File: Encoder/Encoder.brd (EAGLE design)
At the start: 100 x 80 mm, 4 parts, among them IC1 4017D

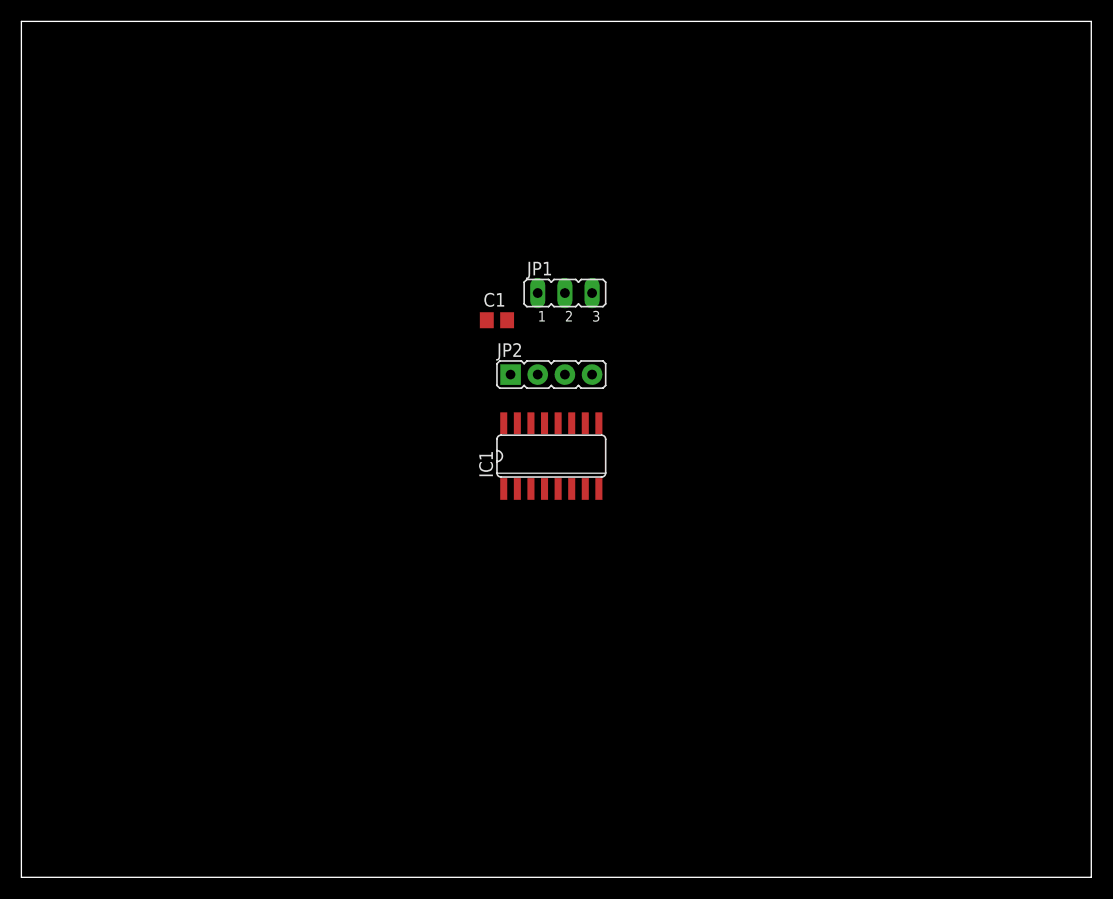
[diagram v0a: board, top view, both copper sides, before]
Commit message: Added a pcb for encoder: made scheme, library and prearranged components on the board
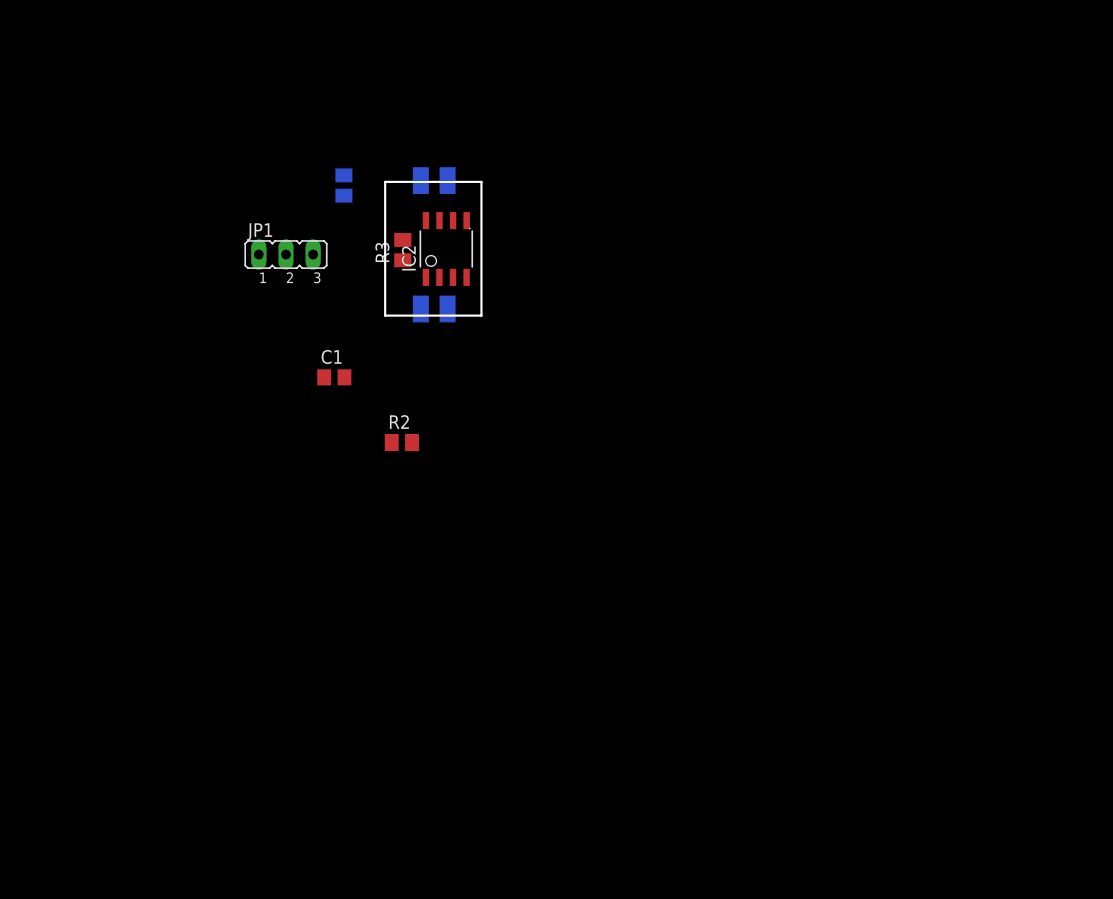
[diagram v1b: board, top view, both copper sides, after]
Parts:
- removed IC1: 4017D, 40xx:SO16
- removed JP2: PLS-(1х4), jumper:PLS-(1х4)
- added IC2: TINY13-20SSU, atmel:8S1
- added R1: (no value), rcl:M0805
- added R2, R3: 10k, rcl:M0805
- added U$1: ITR-9608, EncoderLib:ITR-9608-FOOTPRINT
- C1: value (none) -> 0.1u
- moved JP1 26.3 mm to (24.7, 58.2)
- moved C1 16.1 mm to (29.2, 46.7)
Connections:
- removed net VDD: IC1.16
- removed net VSS: IC1.8
- new net !RES: IC2.1, R3.1
- new net +5V: C1.1, IC2.8, JP1.3, R1.2, R2.2, R3.2
- new net DATA-IN: IC2.5, R2.1, U$1.C
- new net DATA-OUT: IC2.3, JP1.2
- new net GND: C1.2, IC2.4, JP1.1, U$1.E, U$1.K
- new net N$2: R1.1, U$1.A
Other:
- board size 100 x 80 mm -> 9 x 12.5 mm
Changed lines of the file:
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@@
 <setting verticaltext="up"/>
 </settings>
-<grid distance="50" unitdist="mil" unit="mil" style="lines" multiple="1" display="no" altdistance="5" altunitdist="mil" altunit="mil"/>
+<grid distance="0.003125" unitdist="mic" unit="mm" style="lines" multiple="1" display="no" altdistance="5" altunitdist="mil" altunit="mil"/>
 <layers>
 <layer number="1" name="Top" color="4" fill="1" visible="yes" active="yes"/>
@@
 <board>
 <plain>
-<wire x1="0" y1="0" x2="100" y2="0" width="0" layer="20"/>
-<wire x1="100" y1="0" x2="100" y2="80" width="0" layer="20"/>
-<wire x1="100" y1="80" x2="0" y2="80" width="0" layer="20"/>
-<wire x1="0" y1="80" x2="0" y2="0" width="0" layer="20"/>
+<wire x1="0" y1="0" x2="100" y2="0" width="0" layer="49"/>
+<wire x1="100" y1="0" x2="100" y2="80" width="0" layer="49"/>
+<wire x1="100" y1="80" x2="0" y2="80" width="0" layer="49"/>
+<wire x1="0" y1="80" x2="0" y2="0" width="0" layer="49"/>
+<wire x1="34" y1="65" x2="43" y2="65" width="0.2" layer="20"/>
+<wire x1="34" y1="52.5" x2="34" y2="65" width="0.2" layer="20"/>
+<wire x1="43" y1="65" x2="43" y2="52.5" width="0.2" layer="20"/>
+<wire x1="43" y1="52.5" x2="34" y2="52.5" width="0.2" layer="20"/>
 </plain>
 <attributes>
@@
 </autorouter>
 <elements>
-<element name="C1" library="rcl" library_urn="urn:adsk.eagle:library:334" package="C0805" package3d_urn="urn:adsk.eagle:package:23617/2" value="" x="44.45" y="52.07" smashed="yes">
-<attribute name="NAME" x="43.18" y="53.34" size="1.27" layer="25"/>
-<attribute name="POPULARITY" value="88" x="68.58" y="34.29" size="1.778" layer="27" display="off"/>
-<attribute name="SPICEPREFIX" value="C" x="68.58" y="34.29" size="1.778" layer="27" display="off"/>
-<attribute name="VALUE" x="43.18" y="49.53" size="1.27" layer="27"/>
-</element>
-<element name="IC1" library="40xx" library_urn="urn:adsk.eagle:library:80" package="SO16" package3d_urn="urn:adsk.eagle:package:821/2" value="4017D" x="49.53" y="39.37" smashed="yes">
-<attribute name="NAME" x="44.069" y="37.338" size="1.27" layer="25" ratio="10" rot="R90"/>
-<attribute name="POPULARITY" value="0" x="68.58" y="34.29" size="1.778" layer="27" display="off"/>
-<attribute name="VALUE" x="45.466" y="38.735" size="1.27" layer="27" ratio="10"/>
-</element>
-<element name="JP1" library="jumper" library_urn="urn:adsk.eagle:library:252" package="JP2" package3d_urn="urn:adsk.eagle:package:15452/1" value="" x="50.8" y="54.61" smashed="yes">
-<attribute name="NAME" x="47.244" y="56.261" size="1.27" layer="25" ratio="10"/>
-<attribute name="POPULARITY" value="34" x="68.58" y="34.29" size="1.778" layer="27" display="off"/>
-<attribute name="VALUE" x="47.244" y="50.292" size="1.27" layer="27" ratio="10"/>
-</element>
-<element name="JP2" library="jumper" package="PLS-(1х4)" value="PLS-(1х4)" x="49.53" y="46.99" smashed="yes">
-<attribute name="NAME" x="44.45" y="48.641" size="1.27" layer="25" ratio="10"/>
-<attribute name="VALUE" x="44.45" y="44.196" size="1.27" layer="27" ratio="10"/>
-</element>
+<element name="C1" library="rcl" library_urn="urn:adsk.eagle:library:334" package="C0805" package3d_urn="urn:adsk.eagle:package:23617/2" value="0.1u" x="29.2483" y="46.72880625" smashed="yes">
+<attribute name="NAME" x="27.9783" y="47.99880625" size="1.27" layer="25"/>
+<attribute name="POPULARITY" value="88" x="53.3783" y="28.94880625" size="1.778" layer="27" display="off"/>
+<attribute name="SPICEPREFIX" value="C" x="53.3783" y="28.94880625" size="1.778" layer="27" display="off"/>
+<attribute name="VALUE" x="27.9783" y="44.18880625" size="1.27" layer="27"/>
+</element>
+<element name="JP1" library="jumper" library_urn="urn:adsk.eagle:library:252" package="JP2" package3d_urn="urn:adsk.eagle:package:15452/1" value="" x="24.729278125" y="58.20860625" smashed="yes">
+<attribute name="NAME" x="21.173278125" y="59.85960625" size="1.27" layer="25" ratio="10"/>
+<attribute name="POPULARITY" value="34" x="42.509278125" y="37.88860625" size="1.778" layer="27" display="off"/>
+<attribute name="VALUE" x="21.173278125" y="53.89060625" size="1.27" layer="27" ratio="10"/>
+</element>
+<element name="R1" library="rcl" library_urn="urn:adsk.eagle:library:334" package="M0805" package3d_urn="urn:adsk.eagle:package:23556/2" value="" x="30.141446875" y="64.663434375" smashed="yes" rot="MR270">
+<attribute name="NAME" x="28.871446875" y="65.933434375" size="1.27" layer="26" rot="MR270"/>
+<attribute name="POPULARITY" value="45" x="30.141446875" y="64.663434375" size="1.778" layer="28" rot="MR270" display="off"/>
+<attribute name="SPICEPREFIX" value="R" x="30.141446875" y="64.663434375" size="1.778" layer="28" rot="MR270" display="off"/>
+<attribute name="VALUE" x="32.681446875" y="65.933434375" size="1.27" layer="28" rot="MR270"/>
+</element>
+<element name="R2" library="rcl" library_urn="urn:adsk.eagle:library:334" package="M0805" package3d_urn="urn:adsk.eagle:package:23556/2" value="10k" x="35.56" y="40.64" smashed="yes">
+<attribute name="NAME" x="34.29" y="41.91" size="1.27" layer="25"/>
+<attribute name="POPULARITY" value="45" x="35.56" y="40.64" size="1.778" layer="27" display="off"/>
+<attribute name="SPICEPREFIX" value="R" x="35.56" y="40.64" size="1.778" layer="27" display="off"/>
+<attribute name="VALUE" x="34.29" y="38.1" size="1.27" layer="27"/>
+</element>
+<element name="IC2" library="atmel" library_urn="urn:adsk.eagle:library:105" package="8S1" package3d_urn="urn:adsk.eagle:package:4358/1" value="TINY13-20SSU" x="39.714259375" y="58.7253" smashed="yes">
+<attribute name="MF" value="" x="39.714259375" y="58.7253" size="1.778" layer="27" display="off"/>
+<attribute name="MPN" value="ATTINY13-20SSU" x="39.714259375" y="58.7253" size="1.778" layer="27" display="off"/>
+<attribute name="NAME" x="36.856759375" y="56.5663" size="1.27" layer="25" ratio="10" rot="R90"/>
+<attribute name="OC_FARNELL" value="1455133" x="39.714259375" y="58.7253" size="1.778" layer="27" display="off"/>
+<attribute name="OC_NEWARK" value="58M3771" x="39.714259375" y="58.7253" size="1.778" layer="27" display="off"/>
+<attribute name="POPULARITY" value="0" x="39.714259375" y="58.7253" size="1.778" layer="27" display="off"/>
+<attribute name="VALUE" x="43.778259375" y="56.5663" size="1.27" layer="27" ratio="10" rot="R90"/>
+</element>
+<element name="R3" library="rcl" library_urn="urn:adsk.eagle:library:334" package="M0805" package3d_urn="urn:adsk.eagle:package:23556/2" value="10k" x="35.646875" y="58.621234375" smashed="yes" rot="R90">
+<attribute name="NAME" x="34.376875" y="57.351234375" size="1.27" layer="25" rot="R90"/>
+<attribute name="POPULARITY" value="45" x="35.646875" y="58.621234375" size="1.778" layer="27" rot="R90" display="off"/>
+<attribute name="SPICEPREFIX" value="R" x="35.646875" y="58.621234375" size="1.778" layer="27" rot="R90" display="off"/>
+<attribute name="VALUE" x="38.186875" y="57.351234375" size="1.27" layer="27" rot="R90"/>
+</element>
+<element name="U$1" library="EncoderLib" package="ITR-9608-FOOTPRINT" value="ITR-9608" x="38.584378125" y="59.12145625" smashed="yes" rot="MR0"/>
 </elements>
 <signals>
-<signal name="VSS">
-<contactref element="IC1" pad="8"/>
-</signal>
-<signal name="VDD">
-<contactref element="IC1" pad="16"/>
+<signal name="+5V">
+<contactref element="JP1" pad="3"/>
+<contactref element="R1" pad="2"/>
+<contactref element="R2" pad="2"/>
+<contactref element="R3" pad="2"/>
+<contactref element="IC2" pad="8"/>
+<contactref element="C1" pad="1"/>
+<wire x1="35.646875" y1="59.571234375" x2="37.809259375" y2="61.3793" width="0" layer="19" extent="1-1"/>
+<wire x1="27.269278125" y1="58.20860625" x2="35.646875" y2="59.571234375" width="0" layer="19" extent="1-1"/>
+<wire x1="28.2983" y1="46.72880625" x2="27.269278125" y2="58.20860625" width="0" layer="19" extent="1-1"/>
+<wire x1="36.51" y1="40.64" x2="28.2983" y2="46.72880625" width="0" layer="19" extent="1-1"/>
+<wire x1="30.141446875" y1="63.713434375" x2="36.51" y2="40.64" width="0" layer="19" extent="1-16"/>
+</signal>
+<signal name="GND">
+<contactref element="JP1" pad="1"/>
+<contactref element="IC2" pad="4"/>
+<contactref element="C1" pad="2"/>
+<contactref element="U$1" pad="K"/>
+<contactref element="U$1" pad="E"/>
+<wire x1="37.334378125" y1="53.12145625" x2="39.834378125" y2="65.12145625" width="0" layer="19" extent="16-16"/>
+<wire x1="41.609259375" y1="56.0713" x2="37.334378125" y2="53.12145625" width="0" layer="19" extent="1-16"/>
+<wire x1="30.1983" y1="46.72880625" x2="41.609259375" y2="56.0713" width="0" layer="19" extent="1-1"/>
+<wire x1="22.189278125" y1="58.20860625" x2="30.1983" y2="46.72880625" width="0" layer="19" extent="1-1"/>
+</signal>
+<signal name="N$2">
+<contactref element="R1" pad="1"/>
+<contactref element="U$1" pad="A"/>
+<wire x1="30.141446875" y1="65.613434375" x2="37.334378125" y2="65.12145625" width="0" layer="19" extent="16-16"/>
+</signal>
+<signal name="DATA-IN">
+<contactref element="R2" pad="1"/>
+<contactref element="U$1" pad="C"/>
+<contactref element="IC2" pad="5"/>
+<wire x1="39.834378125" y1="53.12145625" x2="41.619259375" y2="61.3793" width="0" layer="19" extent="1-16"/>
+<wire x1="34.61" y1="40.64" x2="39.834378125" y2="53.12145625" width="0" layer="19" extent="1-16"/>
+</signal>
+<signal name="!RES">
+<contactref element="R3" pad="1"/>
+<contactref element="IC2" pad="1"/>
+<wire x1="37.809259375" y1="56.0713" x2="35.646875" y2="57.671234375" width="0" layer="19" extent="1-1"/>
+</signal>
+<signal name="DATA-OUT">
+<contactref element="IC2" pad="3"/>
+<contactref element="JP1" pad="2"/>
+<wire x1="24.729278125" y1="58.20860625" x2="40.339259375" y2="56.0713" width="0" layer="19" extent="1-1"/>
 </signal>
 </signals>
